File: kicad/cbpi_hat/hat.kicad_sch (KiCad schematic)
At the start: 37 parts, among them J1 GPIO, J2 Screw_Terminal_01x02, Q1 HY15P03C2, Q2 DMG2305UX, Q3 DMMT5401-7-F, U1 CAT24C256, U2 EUP3453WIR1, U3 DS3231MZ

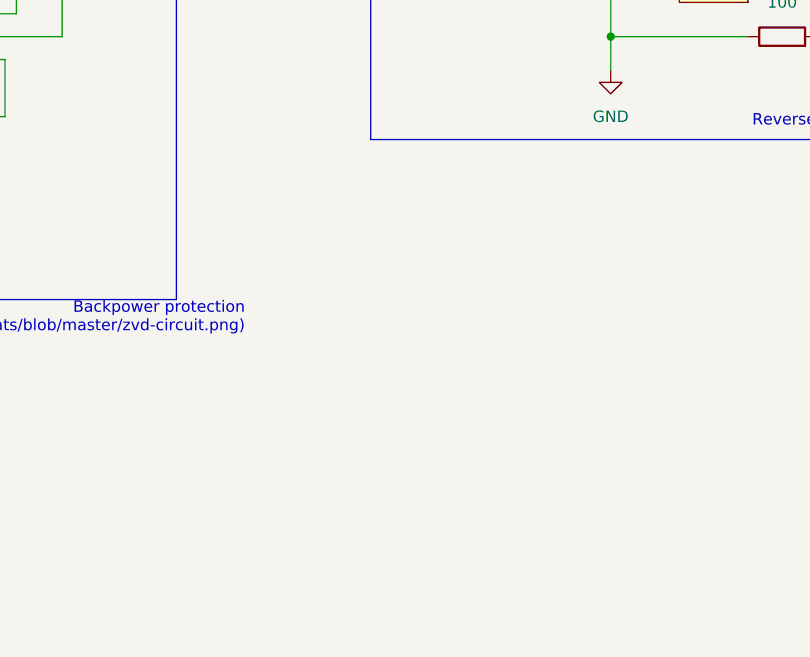
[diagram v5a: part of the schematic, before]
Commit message: Added power and warning LED. This should address #13 and fix it
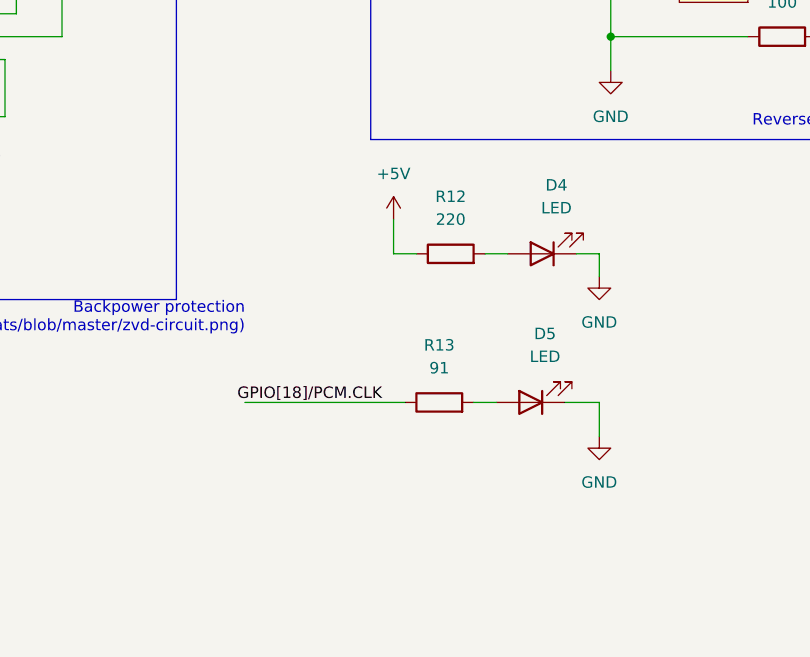
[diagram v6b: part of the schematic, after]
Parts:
- added D4, D5: LED, LED_SMD:LED_0603_1608Metric, symbol Device:LED
- added R12: 220, Resistor_SMD:R_0402_1005Metric, symbol Device:R
- added R13: 91, Resistor_SMD:R_0402_1005Metric, symbol Device:R
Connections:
- net +5V: now also R12.1
- net GND: now also D4.1 (K), D5.1 (K)
- net GPIO[18]/PCM.CLK: now also R13.1
- new net: D5.2 (A), R13.2
- new net: D4.2 (A), R12.2
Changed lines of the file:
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@@
+    (stroke (width 0) (type default) (color 0 0 0 0))
+  )
+  (wire (pts (xy 294.64 66.04) (xy 297.18 66.04))
     (stroke (width 0) (type default) (color 0 0 0 0))
   )
@@
     (stroke (width 0) (type default) (color 0 0 0 0))
   )
+  (wire (pts (xy 314.96 66.04) (xy 317.5 66.04))
+    (stroke (width 0) (type default) (color 0 0 0 0))
+  )
   (wire (pts (xy 471.17 63.5) (xy 463.55 63.5))
     (stroke (width 0) (type default) (color 0 0 0 0))
@@
     (stroke (width 0) (type default) (color 0 0 0 0))
   )
+  (wire (pts (xy 294.64 62.23) (xy 294.64 66.04))
+    (stroke (width 0) (type default) (color 0 0 0 0))
+  )
   (polyline (pts (xy 217.17 13.97) (xy 270.51 13.97))
     (stroke (width 0) (type default) (color 0 0 0 0))
@@
     (stroke (width 0) (type default) (color 0 0 0 0))
   )
+  (wire (pts (xy 304.8 66.04) (xy 307.34 66.04))
+    (stroke (width 0) (type default) (color 0 0 0 0))
+  )
   (wire (pts (xy 31.75 53.34) (xy 60.96 53.34))
     (stroke (width 0) (type solid) (color 0 0 0 0))
@@
     (stroke (width 0) (type default) (color 0 0 0 0))
   )
+  (wire (pts (xy 317.5 82.55) (xy 317.5 86.36))
+    (stroke (width 0) (type default) (color 0 0 0 0))
+  )
   (wire (pts (xy 73.66 71.12) (xy 100.33 71.12))
     (stroke (width 0) (type solid) (color 0 0 0 0))
@@
     (stroke (width 0) (type default) (color 0 0 0 0))
   )
+  (wire (pts (xy 278.13 82.55) (xy 295.91 82.55))
+    (stroke (width 0) (type default) (color 0 0 0 0))
+  )
+  (wire (pts (xy 317.5 66.04) (xy 317.5 68.58))
+    (stroke (width 0) (type default) (color 0 0 0 0))
+  )
   (wire (pts (xy 133.35 30.48) (xy 133.35 33.02))
     (stroke (width 0) (type default) (color 0 0 0 0))
@@
     (stroke (width 0) (type default) (color 0 0 0 0))
   )
+  (wire (pts (xy 303.53 82.55) (xy 306.07 82.55))
+    (stroke (width 0) (type default) (color 0 0 0 0))
+  )
   (wire (pts (xy 76.2 63.5) (xy 73.66 63.5))
     (stroke (width 0) (type solid) (color 0 0 0 0))
@@
   )
   (wire (pts (xy 127 52.07) (xy 127 62.23))
+    (stroke (width 0) (type default) (color 0 0 0 0))
+  )
+  (wire (pts (xy 313.69 82.55) (xy 317.5 82.55))
     (stroke (width 0) (type default) (color 0 0 0 0))
   )
@@
   (label "24V_PRE_PP" (at 320.04 25.4 0)
     (effects (font (size 1.27 1.27)) (justify left bottom))
+  )
+  (label "GPIO[18]{slash}PCM.CLK" (at 293.37 82.55 180)
+    (effects (font (size 1.27 1.27)) (justify right bottom))
   )
   (label "ID_SDA" (at 110.49 175.26 180)
@@
     (pin "1")
   )
+  (symbol (lib_id "power:+5V") (at 294.64 62.23 0) (unit 1)
+    (in_bom yes) (on_board yes) (fields_autoplaced)
+    (property "Reference" "#PWR01" (id 0) (at 294.64 66.04 0)
+      (effects (font (size 1.27 1.27)) hide)
+    )
+    (property "Value" "+5V" (id 1) (at 294.64 57.15 0))
+    (property "Footprint" "" (id 2) (at 294.64 62.23 0)
+      (effects (font (size 1.27 1.27)) hide)
+    )
+    (property "Datasheet" "" (id 3) (at 294.64 62.23 0)
+      (effects (font (size 1.27 1.27)) hide)
+    )
+    (pin "1")
+  )
   (symbol (lib_id "Device:R") (at 463.55 58.42 0) (unit 1)
     (in_bom yes) (on_board yes) (fields_autoplaced)
@@
     (pin "2")
   )
+  (symbol (lib_id "power:GND") (at 317.5 86.36 0) (unit 1)
+    (in_bom yes) (on_board yes) (fields_autoplaced)
+    (property "Reference" "#PWR06" (id 0) (at 317.5 92.71 0)
+      (effects (font (size 1.27 1.27)) hide)
+    )
+    (property "Value" "GND" (id 1) (at 317.5 91.44 0))
+    (property "Footprint" "" (id 2) (at 317.5 86.36 0)
+      (effects (font (size 1.27 1.27)) hide)
+    )
+    (property "Datasheet" "" (id 3) (at 317.5 86.36 0)
+      (effects (font (size 1.27 1.27)) hide)
+    )
+    (pin "1")
+  )
   (symbol (lib_id "power:+3.3V") (at 101.6 162.56 0) (unit 1)
     (in_bom yes) (on_board yes)
@@
     (pin "1")
   )
+  (symbol (lib_id "Device:LED") (at 309.88 82.55 180) (unit 1)
+    (in_bom yes) (on_board yes) (fields_autoplaced)
+    (property "Reference" "D5" (id 0) (at 311.4675 74.93 0))
+    (property "Value" "LED" (id 1) (at 311.4675 77.47 0))
+    (property "Footprint" "LED_SMD:LED_0603_1608Metric" (id 2) (at 309.88 82.55 0)
+      (effects (font (size 1.27 1.27)) hide)
+    )
+    (property "Datasheet" "~" (id 3) (at 309.88 82.55 0)
+      (effects (font (size 1.27 1.27)) hide)
+    )
+    (pin "1")
+    (pin "2")
+  )
   (symbol (lib_id "Device:R") (at 459.74 44.45 0) (unit 1)
     (in_bom yes) (on_board yes) (fields_autoplaced)
@@
     )
     (pin "1")
+  )
+  (symbol (lib_id "Device:R") (at 300.99 66.04 90) (unit 1)
+    (in_bom yes) (on_board yes) (fields_autoplaced)
+    (property "Reference" "R12" (id 0) (at 300.99 59.69 90))
+    (property "Value" "220" (id 1) (at 300.99 62.23 90))
+    (property "Footprint" "Resistor_SMD:R_0402_1005Metric" (id 2) (at 300.99 67.818 90)
+      (effects (font (size 1.27 1.27)) hide)
+    )
+    (property "Datasheet" "~" (id 3) (at 300.99 66.04 0)
+      (effects (font (size 1.27 1.27)) hide)
+    )
+    (pin "1")
+    (pin "2")
   )
   (symbol (lib_id "Memory_EEPROM:CAT24C256") (at 81.28 177.8 0) (unit 1)
@@
     (pin "1")
   )
+  (symbol (lib_id "power:GND") (at 317.5 68.58 0) (unit 1)
+    (in_bom yes) (on_board yes) (fields_autoplaced)
+    (property "Reference" "#PWR05" (id 0) (at 317.5 74.93 0)
+      (effects (font (size 1.27 1.27)) hide)
+    )
+    (property "Value" "GND" (id 1) (at 317.5 73.66 0))
+    (property "Footprint" "" (id 2) (at 317.5 68.58 0)
+      (effects (font (size 1.27 1.27)) hide)
+    )
+    (property "Datasheet" "" (id 3) (at 317.5 68.58 0)
+      (effects (font (size 1.27 1.27)) hide)
+    )
+    (pin "1")
+  )
   (symbol (lib_id "power:PWR_FLAG") (at 133.35 30.48 0) (unit 1)
     (in_bom yes) (on_board yes) (fields_autoplaced)
@@
     )
     (pin "1")
+  )
+  (symbol (lib_id "Device:LED") (at 311.15 66.04 180) (unit 1)
+    (in_bom yes) (on_board yes) (fields_autoplaced)
+    (property "Reference" "D4" (id 0) (at 312.7375 58.42 0))
+    (property "Value" "LED" (id 1) (at 312.7375 60.96 0))
+    (property "Footprint" "LED_SMD:LED_0603_1608Metric" (id 2) (at 311.15 66.04 0)
+      (effects (font (size 1.27 1.27)) hide)
+    )
+    (property "Datasheet" "~" (id 3) (at 311.15 66.04 0)
+      (effects (font (size 1.27 1.27)) hide)
+    )
+    (pin "1")
+    (pin "2")
+  )
+  (symbol (lib_id "Device:R") (at 299.72 82.55 90) (unit 1)
+    (in_bom yes) (on_board yes) (fields_autoplaced)
+    (property "Reference" "R13" (id 0) (at 299.72 76.2 90))
+    (property "Value" "91" (id 1) (at 299.72 78.74 90))
+    (property "Footprint" "Resistor_SMD:R_0402_1005Metric" (id 2) (at 299.72 84.328 90)
+      (effects (font (size 1.27 1.27)) hide)
+    )
+    (property "Datasheet" "~" (id 3) (at 299.72 82.55 0)
+      (effects (font (size 1.27 1.27)) hide)
+    )
+    (pin "1")
+    (pin "2")
   )
   (symbol (lib_id "hy15p03c2:HY15P03C2") (at 330.2 30.48 180) (unit 1)
@@
       (reference "#FLG0107") (unit 1) (value "PWR_FLAG") (footprint "")
     )
+    (path "/1a686870-87ee-4fc2-8a93-4b4d5a2bbeb7"
+      (reference "#PWR01") (unit 1) (value "+5V") (footprint "")
+    )
     (path "/00000000-0000-0000-0000-0000580c1d11"
       (reference "#PWR02") (unit 1) (value "GND") (footprint "")
@@
       (reference "#PWR04") (unit 1) (value "+3.3V") (footprint "")
     )
+    (path "/b59e453c-761c-43b3-862c-b2f9f74bc76b"
+      (reference "#PWR05") (unit 1) (value "GND") (footprint "")
+    )
+    (path "/5195b16f-c457-4ed8-bdbf-d1ac07644a9e"
+      (reference "#PWR06") (unit 1) (value "GND") (footprint "")
+    )
     (path "/55bbe0f6-d435-4137-8361-5f963fa98019"
       (reference "#PWR0101") (unit 1) (value "+3.3V") (footprint "")
@@
       (reference "D3") (unit 1) (value "MM1Z9V1") (footprint "Diode_SMD:D_SOD-123")
     )
+    (path "/cb037949-d212-4d4f-a3c8-5f0d82f7d8e9"
+      (reference "D4") (unit 1) (value "LED") (footprint "LED_SMD:LED_0603_1608Metric")
+    )
+    (path "/5b27af5f-0a76-4e5c-b37c-7f4cf6b4c798"
+      (reference "D5") (unit 1) (value "LED") (footprint "LED_SMD:LED_0603_1608Metric")
+    )
     (path "/21acbfdc-e37e-4cbd-ba10-26cc1460c0ae"
       (reference "F1") (unit 1) (value "Fuse") (footprint "Fuse:Fuse_Blade_ATO_directSolder")
@@
       (reference "R11") (unit 1) (value "47k") (footprint "Resistor_SMD:R_0402_1005Metric")
     )
+    (path "/6897c4af-c200-4691-881a-b56923373f82"
+      (reference "R12") (unit 1) (value "220") (footprint "Resistor_SMD:R_0402_1005Metric")
+    )
+    (path "/cd17d4b1-50fd-44a5-830a-463a0025bf85"
+      (reference "R13") (unit 1) (value "91") (footprint "Resistor_SMD:R_0402_1005Metric")
+    )
     (path "/6d6e5c8e-c0cf-4e61-9c00-723a754d58be"

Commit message: Replaced CR2032 holder with the old more space saving one and fixed all DRC errors and warnings except for unconnected GND
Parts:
- BT1: footprint cr2032-bs-6-1:BAT-TH_CR2032-BS-6-1 -> cr2032-bs-5-1:BAT-TH_CR2032-BS-5-1
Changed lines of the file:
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@@
       (effects (font (size 1.27 1.27)) (justify left))
     )
-    (property "Footprint" "cr2032-bs-6-1:BAT-TH_CR2032-BS-6-1" (id 2) (at 127 48.006 90)
+    (property "Footprint" "cr2032-bs-5-1:BAT-TH_CR2032-BS-5-1" (id 2) (at 127 48.006 90)
       (effects (font (size 1.27 1.27)) hide)
     )
@@
     )
     (path "/4c443932-87d8-4252-a612-8cadafc00eb7"
-      (reference "BT1") (unit 1) (value "Battery_Cell") (footprint "cr2032-bs-6-1:BAT-TH_CR2032-BS-6-1")
+      (reference "BT1") (unit 1) (value "Battery_Cell") (footprint "cr2032-bs-5-1:BAT-TH_CR2032-BS-5-1")
     )
     (path "/0f7872a7-de47-41d5-a21f-9934102d3a5f"
